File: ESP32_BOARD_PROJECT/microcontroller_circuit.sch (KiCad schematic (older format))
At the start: 3 parts

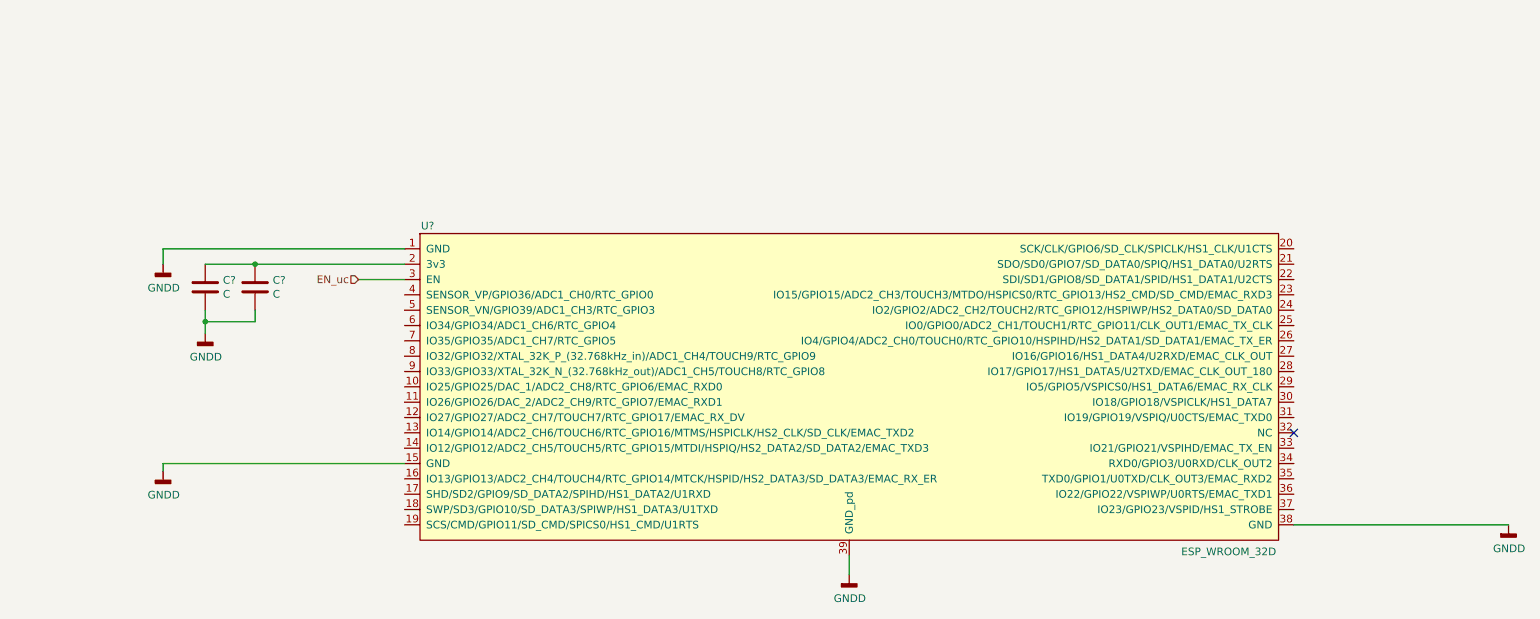
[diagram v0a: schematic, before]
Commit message: USB-Serial converter circuit half done
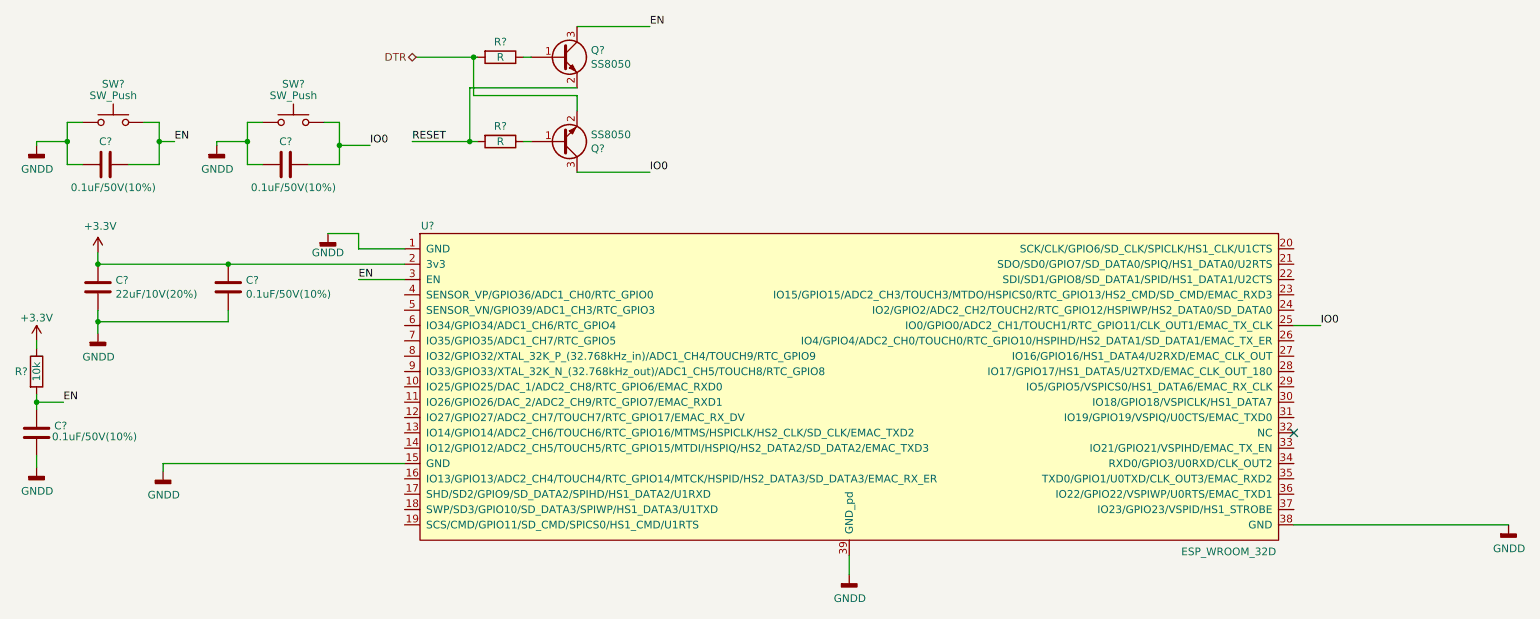
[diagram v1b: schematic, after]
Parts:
- added C? (x3): 0.1uF/50V(10%), symbol Device:C
- added Q? (x2): SS8050, Package_TO_SOT_SMD:SOT-23, symbol ESP_BOARD_IOT_PROJECT:SS8050
- added R?: 10k, symbol Device:R
- added R? (x2): R, symbol Device:R
- added SW? (x2): SW_Push, symbol Switch:SW_Push
- C?: value C -> 22uF/10V(20%)
- C?: value C -> 0.1uF/50V(10%)
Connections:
- net GNDD: now also C?.2, C?.2, C?.2, SW?.1, SW?.1
- net +3V3: now reaches C?.1, C?.1, U?.2 (3v3)
- net +3V3: now also R?.1
- net IO0: now reaches U?.25 (IO0/GPIO0/ADC2_CH1/TOUCH1/RTC_GPIO11/CLK_OUT1/EMAC_TX_CLK)
- net IO0: now also C?.1, Q?.3 (C), SW?.2
- net EN_uc renamed EN
- net EN: now also C?.1, C?.1, Q?.3 (C), R?.2, SW?.2
- new net: Q?.1 (B), R?.1 (x2)
- new net DTR: Q?.2 (E), R?.2
- new net RESET: Q?.2 (E), R?.2
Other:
- moved on the sheet: C?
